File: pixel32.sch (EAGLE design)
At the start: 63 parts, among them CON1 DS1066-07M-SIDE, CON2 DS1066-07M-SIDE, CON3 PINHEAD_1X02-2.54, IC1 STM32F030K6TX-LQFP32(7X7), IC2 TPS54260, IC3 ST3485SOIC8, IC4 ESDA6V1L, IC5 3.3, IC6 MC74VHC1GT125, IC7 MC74VHC1GT125

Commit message: BLAH
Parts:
- removed C22: 1nF 1000V, rc:C-1206
- removed C25: 10uF 6.3V, rc:C-1206
- removed D4: SMF05C, pixel_masterlib:SMF05C
- removed D5: SMAJ12A, masterlib:SMAJ12A
- removed IC4: ESDA6V1L, pixel_masterlib:ESDA6V1L
- removed NRF24L01: NRF24L01, ali_modules:NRF24L01
- removed SJ1: (no value), eth_conv_master_lib:SOLDER_JOINT
- added C18: 100 nF, rc:C-0603
- added C27: 4.7u, rc:C-0805
- added C28: 0.1u, rc:C-0805
- added D1: SMF05C, pixel_masterlib:SMF05C
- added IC8: LM317, masterlib:LM317
- added R10, R13: (no value), rc:R-0805
- added R14, R15: 10K, rc:R-0603
- added SJ3, SJ4: (no value), eth_conv_master_lib:SOLDER_JOINT
- added U$6: CONNECTION, usb2can_master_lib:CONNECTION
- R11, R12: value 22R -> 100R
- R5: value 60R -> 120R
- R6: value 560R -> 1K; device rc:R-0603 -> rc:R-0805
- R7: value 560R -> 5K6; device rc:R-0603 -> rc:R-0805
- R9: value 60R -> 10K
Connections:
- removed net N$16: R5.1, R9.2, SJ1.1
- removed net N$17: C22.1, SJ1.2
- removed net N$18: R9.1, SJ2.2
- removed net NRF_CE: NRF24L01.CE
- removed net NRF_CSN: NRF24L01.CSN
- removed net NRF_IRQ: NRF24L01.IRQ
- new net GNDD: CON1.7, CON2.7, U$6.P$1
- new net LED_ANODE: C1.2, D1.C
- new net N$1: R5.1, SJ2.2
- new net N$20: IC8.ADJ, R6.1, R7.2
- new net VIN_SENSE: C18.2, R10.2, R13.2
- net A: now also D1.D2; no longer D5.P$1, IC4.C1, R6.2
- net B: now also D1.D1; no longer D5.P$2, IC4.C2, R7.1
- net CLOCK: now also D1.D4; no longer D4.D4, NRF24L01.SCK
- net CS: now also D1.D5; no longer D4.D5
- net CURRENT_SENS: no longer C1.1
- net DATA: now also D1.D3; no longer D4.D3
- net GND: now also C18.1, C27.1, C28.1, D1.G, R13.1, R14.1, R15.1, R7.1, R9.1, U$6.P$2; no longer C22.2, C25.2, CON1.7, CON2.7, D4.G, IC4.A, NRF24L01.GND, R6.1
- net LED1_PWM: now also R9.2
- net LED2_PWM: now also R14.2
- net LED3_PWM: now also R15.2
- net LED_CATHODE: now also C1.1; no longer C1.2
- net MISO: no longer NRF24L01.MISO
- net MOSI/DATA: no longer NRF24L01.MOSI
- net N$2: now also D1.A
- net N$3: now also LED_ANODE.P, R10.1, SJ3.1, SJ4.2
- net RS485_A: now also R12.2; no longer R11.2
- net RS485_B: now also R11.2; no longer R12.2
- net VDD_12V: now also C27.2, IC8.OUT, R6.2, SJ3.2; no longer LED_ANODE.P
- net VDD_24V: now also C28.2, IC8.IN, SJ4.1
- net VDD_3V3: no longer C25.1, NRF24L01.VCC, R7.2
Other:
- note added: "8.25V output"
- note removed: "OPTIONAL NRF24L01"
- moved on the sheet: C26, C5, C6, CON3, D3, LED_ANODE, LED_CATHODE1, LED_CATHODE2, LED_CATHODE3, R11, R12, R8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

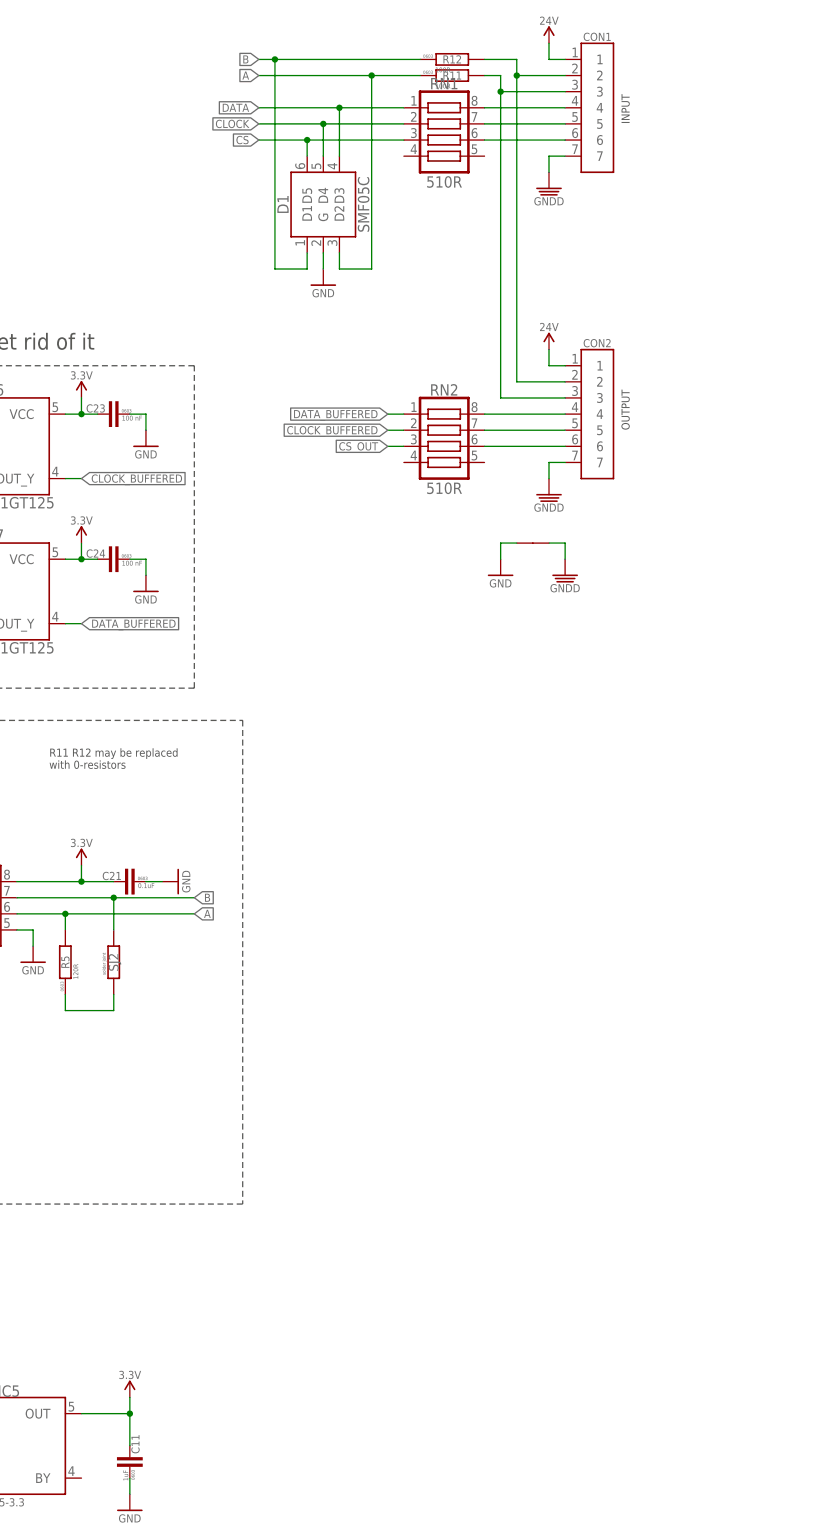
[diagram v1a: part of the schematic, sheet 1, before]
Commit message: First attempts in routing
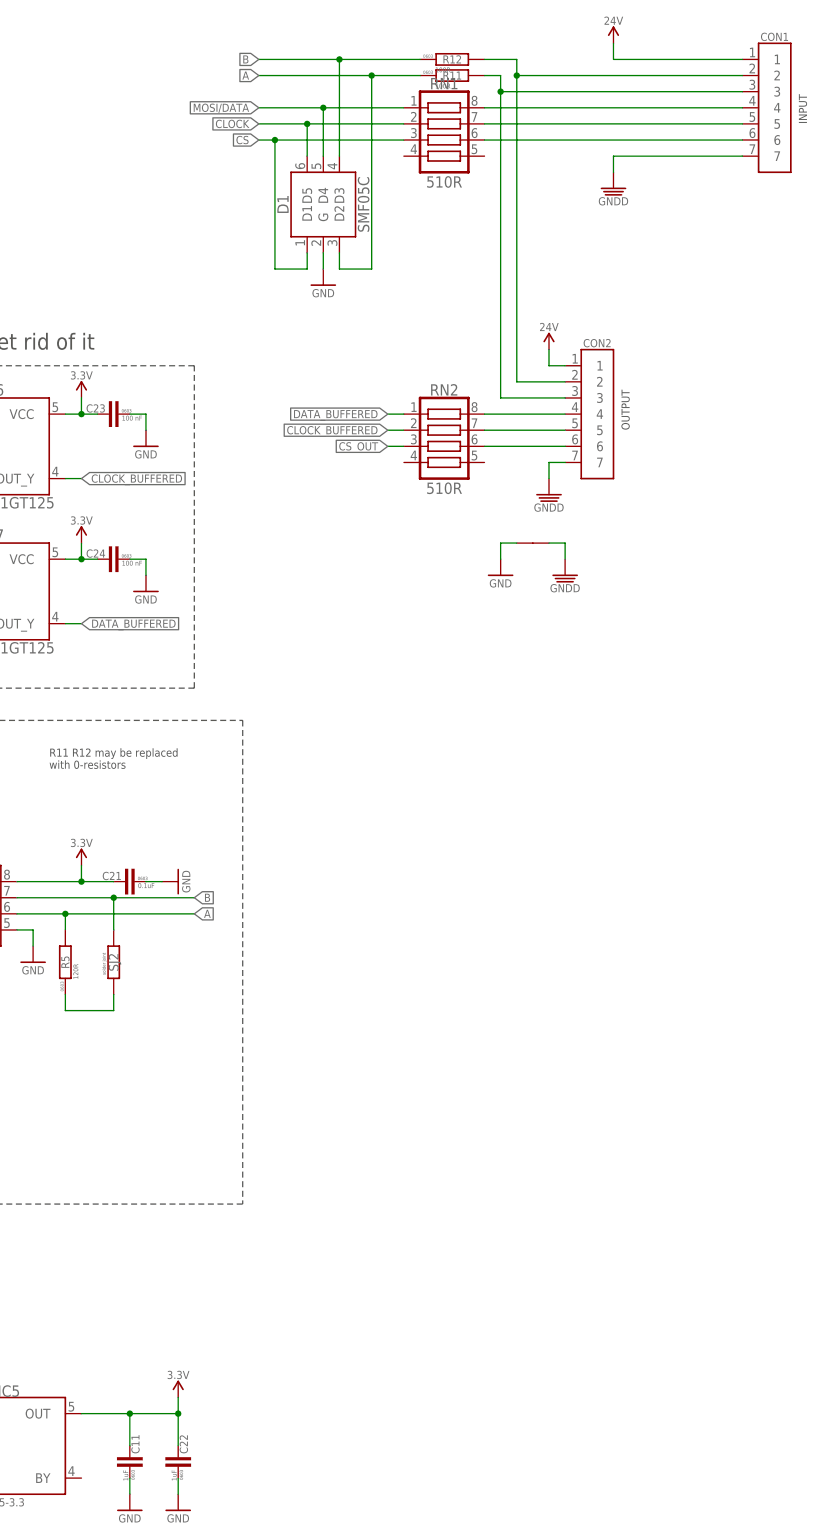
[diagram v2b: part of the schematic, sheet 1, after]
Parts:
- added C22: 1uF, rc:C-0603
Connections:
- removed net DATA: D1.D3, RN1.1
- net B: now also D1.D3; no longer D1.D1
- net CLOCK: now also D1.D5; no longer D1.D4
- net CS: now also D1.D1; no longer D1.D5
- net GND: now also C22.1
- net MOSI/DATA: now also D1.D4, RN1.1
- net VDD_3V3: now also C22.2
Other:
- moved on the sheet: CON1

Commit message: blah
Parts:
- removed C1: 0.1uF, rc:C-0603
- removed C10, C11, C22: 1uF, rc:C-0603
- removed C2, C3: 4.7u, rc:C-1210
- removed C4: 10n, rc:C-0603
- removed C5, C6: 47u 16V, rc:C-1210
- removed C7, C8: 18pF, rc:C-0603
- removed C9: 4700p, rc:C-0603
- removed D3: B360B-SMB, eth_conv_master_lib:B360B-SMB
- removed IC2: TPS54260, eth_conv_master_lib:TPS54260
- removed IC5: 3.3, gradus_mater_lib:LP2985-3.3V
- removed L1: 3R3, eth_conv_master_lib:L
- removed R1: 100K, rc:R-0603
- removed R2, R3: XXX, rc:R-0603
- removed R4: 18K 1%, rc:R-0603
- removed SJ4: (no value), eth_conv_master_lib:SOLDER_JOINT
- added SJ1: (no value), eth_conv_master_lib:SOLDER_JOINT
- C27, C28: device rc:C-0805 -> rc:C-1206
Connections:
- removed net AA: C1.2, D3.C, IC2.PH, L1.P$1
- removed net CURRENT_SENS: C3.2, R2.2
- removed net FB: IC2.VSENSE, R2.2, R3.1
- removed net LED_CATHODE: C1.1
- removed net N$6: C4.2, IC2.SS/TR
- removed net N$7: IC2.RT/CLK, R1.2
- removed net N$8: C9.2, R4.1
- net CLOCK: now also RN1.3; no longer RN1.2
- net CS: now also RN1.4; no longer RN1.3
- net CS_OUT: now also IC1.PA11, RN2.4; no longer IC1.PB6, RN2.3
- net GND: no longer C10.1, C11.1, C2.1, C22.1, C3.1, C4.1, C5.1, C6.1, C7.2, C8.2, C9.1, D3.A, IC2.GND, IC5.GND, R1.1, R2.1
- net LED_ANODE: no longer C1.2
- net MOSI/DATA: now also RN1.2; no longer RN1.1
- net N$11: now also RN1.7; no longer RN1.8
- net N$12: now also RN1.6; no longer RN1.7
- net N$13: now also RN1.5; no longer RN1.6
- net N$19: now also RN2.5; no longer RN2.6
- net N$2: no longer C1.1, IC2.BOOT
- net N$3: no longer LED_ANODE.P, R1.1, R10.1, R3.2, SJ3.1, SJ4.2
- net N$5: now also C28.2, IC8.IN, SJ1.2, SJ3.2; no longer C7.1, C8.1, IC2.COMP, R4.2
- net PWM: no longer R3.1
- net VDD_12V: now also SJ1.1; no longer C10.2, C2.2, C27.2, C5.2, C6.2, IC5.EN, IC5.IN, IC8.OUT, L1.P$2, R3.2, R6.2, SJ3.2
- net VDD_24V: now also LED_ANODE.P, R10.1, SJ3.1; no longer C2.2, C28.2, C3.2, IC2.VIN, IC8.IN, SJ4.1
- net VDD_3V3: now also C27.2, IC8.OUT, R6.2; no longer C11.2, C22.2, IC5.OUT
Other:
- note removed: "8.25V output"
- note removed: "C7 and C12 are here to reduce BOM"
- note removed: "Only option1 OR option2 should be placed"
- note removed: "Option 2"
- note removed: "Option1 will have max input V 60V"
- note removed: "Option2 will have max input V 25V. But its cheaper and easier"
- note removed: "Pull EN below 1.2V to disable Float to enable"
- note removed: "R11 R12 may be replaced with 0-resistors"
- moved on the sheet: C18, C21, C27, C28, CON1, D1, IC8, MODULE1, R10, R13, R6, R7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

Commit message: blah
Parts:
- removed C12: 100 nF, rc:C-0603
- added CON4: PINHEAD_1X03-2.54, pinhead:PINHEAD_1X03-2.54
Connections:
- removed net SYS_SWCLK: IC1.PA14
- removed net SYS_SWDIO: IC1.PA13
- net CS_OUT: now also IC1.PA12; no longer IC1.PA11
- net GND: now also CON4.2; no longer C12.1
- net N$2: now also CON4.1, IC1.PA14
- net N$3: now also CON4.3, IC1.PA13
- net VDD_3V3: no longer C12.2
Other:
- moved on the sheet: C13
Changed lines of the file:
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@@
 <part name="Q1" library="pixel_masterlib" deviceset="N-FET" device=""/>
 <part name="FRAME1" library="frames" deviceset="A5L-LOC" device=""/>
-<part name="C1" library="rc" deviceset="C" device="-1206" value="100 nF"/>
+<part name="C1" library="rc" deviceset="C" device="-1812" value="100 nF"/>
 </parts>
 <sheets>
@@
 <attribute name="BOM" x="88.9" y="93.98" size="1.778" layer="96" rot="R180" display="off"/>
 </instance>
-<instance part="TP3" gate="G$1" x="88.9" y="73.66" rot="R180">
-<attribute name="PARTNO" x="88.9" y="73.66" size="1.778" layer="96" rot="R180" display="off"/>
-<attribute name="BOM" x="88.9" y="73.66" size="1.778" layer="96" rot="R180" display="off"/>
+<instance part="TP3" gate="G$1" x="86.36" y="73.66" rot="R180">
+<attribute name="PARTNO" x="86.36" y="73.66" size="1.778" layer="96" rot="R180" display="off"/>
+<attribute name="BOM" x="86.36" y="73.66" size="1.778" layer="96" rot="R180" display="off"/>
 </instance>
 <instance part="+P1" gate="G$1" x="30.48" y="99.06"/>
@@
 <junction x="106.68" y="73.66"/>
 <pinref part="TP3" gate="G$1" pin="P$1"/>
-<wire x1="101.6" y1="73.66" x2="96.52" y2="73.66" width="0.1524" layer="91"/>
+<wire x1="101.6" y1="73.66" x2="93.98" y2="73.66" width="0.1524" layer="91"/>
 <pinref part="Q1" gate="G$1" pin="S"/>
 <wire x1="101.6" y1="81.28" x2="101.6" y2="73.66" width="0.1524" layer="91"/>
@@
 <part name="IC1" library="pixel_masterlib" deviceset="STM32F030K6TX" device="-LQFP32(7X7)"/>
 <part name="GND2" library="supply_symbols" deviceset="GND" device="" value="GND"/>
-<part name="C12" library="rc" deviceset="C" device="-0603" value="100 nF"/>
 <part name="C13" library="rc" deviceset="C" device="-0603" value="100 nF"/>
 <part name="C14" library="rc" deviceset="C" device="-0603" value="1 uF"/>
@@
 <part name="+P4" library="supply_symbols" deviceset="12V" device=""/>
 <part name="+P14" library="supply_symbols" deviceset="24V" device=""/>
+<part name="CON4" library="pinhead" deviceset="PINHEAD_1X03" device="-2.54"/>
+<part name="GND1" library="supply_symbols" deviceset="GND" device="" value="GND"/>
 </parts>
 <sheets>
@@
 <instance part="IC1" gate="IC" x="66.04" y="187.96"/>
 <instance part="GND2" gate="1" x="43.18" y="193.04"/>
-<instance part="C12" gate="G$1" x="55.88" y="228.6"/>
-<instance part="C13" gate="G$1" x="55.88" y="223.52"/>
+<instance part="C13" gate="G$1" x="55.88" y="226.06"/>
 <instance part="C14" gate="G$1" x="43.18" y="200.66" rot="R90"/>
 <instance part="C15" gate="G$1" x="48.26" y="200.66" rot="R90"/>
-<instance part="GND5" gate="1" x="50.8" y="218.44"/>
+<instance part="GND5" gate="1" x="50.8" y="220.98"/>
 <instance part="+P5" gate="G$1" x="43.18" y="208.28"/>
 <instance part="GND6" gate="1" x="48.26" y="193.04"/>
@@
 <instance part="R12" gate="G$1" x="322.58" y="241.3"/>
 <instance part="GND26" gate="1" x="256.54" y="99.06"/>
-<instance part="+P9" gate="G$1" x="60.96" y="231.14" rot="MR0"/>
+<instance part="+P9" gate="G$1" x="60.96" y="228.6" rot="MR0"/>
 <instance part="GND29" gate="1" x="274.32" y="96.52"/>
 <instance part="+P10" gate="G$1" x="264.16" y="114.3" rot="MR0"/>
@@
 <instance part="GND22" gate="G$1" x="337.82" y="172.72" rot="MR0"/>
 <instance part="GND23" gate="G$1" x="347.98" y="218.44" rot="MR0"/>
+<instance part="CON4" gate="G$1" x="134.62" y="220.98" rot="R180"/>
+<instance part="GND1" gate="1" x="116.84" y="215.9" rot="MR90"/>
 </instances>
 <busses>
@@
 </segment>
 <segment>
-<pinref part="C12" gate="G$1" pin="2"/>
 <pinref part="C13" gate="G$1" pin="2"/>
 <pinref part="IC1" gate="IC" pin="VDD@1"/>
 <wire x1="63.5" y1="215.9" x2="60.96" y2="215.9" width="0.1524" layer="91"/>
-<wire x1="60.96" y1="215.9" x2="60.96" y2="223.52" width="0.1524" layer="91"/>
+<wire x1="60.96" y1="215.9" x2="60.96" y2="226.06" width="0.1524" layer="91"/>
 <pinref part="+P9" gate="G$1" pin="VDD_3V3"/>
-<wire x1="58.42" y1="228.6" x2="60.96" y2="228.6" width="0.1524" layer="91"/>
-<wire x1="60.96" y1="228.6" x2="60.96" y2="231.14" width="0.1524" layer="91"/>
-<junction x="60.96" y="228.6"/>
-<wire x1="60.96" y1="223.52" x2="60.96" y2="228.6" width="0.1524" layer="91"/>
-<wire x1="58.42" y1="223.52" x2="60.96" y2="223.52" width="0.1524" layer="91"/>
-<junction x="60.96" y="223.52"/>
+<wire x1="60.96" y1="226.06" x2="60.96" y2="228.6" width="0.1524" layer="91"/>
+<wire x1="58.42" y1="226.06" x2="60.96" y2="226.06" width="0.1524" layer="91"/>
+<junction x="60.96" y="226.06"/>
 </segment>
 <segment>
@@
 <pinref part="GND5" gate="1" pin="GND"/>
 <pinref part="C13" gate="G$1" pin="1"/>
-<wire x1="53.34" y1="223.52" x2="50.8" y2="223.52" width="0.1524" layer="91"/>
-<wire x1="50.8" y1="223.52" x2="50.8" y2="220.98" width="0.1524" layer="91"/>
-<pinref part="C12" gate="G$1" pin="1"/>
-<wire x1="53.34" y1="228.6" x2="50.8" y2="228.6" width="0.1524" layer="91"/>
-<wire x1="50.8" y1="228.6" x2="50.8" y2="223.52" width="0.1524" layer="91"/>
-<junction x="50.8" y="223.52"/>
+<wire x1="53.34" y1="226.06" x2="50.8" y2="226.06" width="0.1524" layer="91"/>
+<wire x1="50.8" y1="226.06" x2="50.8" y2="223.52" width="0.1524" layer="91"/>
 </segment>
 <segment>
@@
 <wire x1="330.2" y1="165.1" x2="330.2" y2="162.56" width="0.1524" layer="91"/>
 </segment>
+<segment>
+<pinref part="CON4" gate="G$1" pin="2"/>
+<pinref part="GND1" gate="1" pin="GND"/>
+<wire x1="119.38" y1="215.9" x2="127" y2="215.9" width="0.1524" layer="91"/>
+</segment>
 </net>
 <net name="N$4" class="0">
@@
 <pinref part="RN1" gate="G$1" pin="3"/>
 <wire x1="299.72" y1="228.6" x2="314.96" y2="228.6" width="0.1524" layer="91"/>
-</segment>
-</net>
-<net name="SYS_SWDIO" class="0">
-<segment>
-<pinref part="IC1" gate="IC" pin="PA13"/>
-<wire x1="106.68" y1="213.36" x2="109.22" y2="213.36" width="0.1524" layer="91"/>
-<label x="109.22" y="213.36" size="1.27" layer="95" rot="MR180" xref="yes"/>
-</segment>
-</net>
-<net name="SYS_SWCLK" class="0">
-<segment>
-<pinref part="IC1" gate="IC" pin="PA14"/>
-<wire x1="106.68" y1="215.9" x2="109.22" y2="215.9" width="0.1524" layer="91"/>
-<label x="109.22" y="215.9" size="1.27" layer="95" rot="MR180" xref="yes"/>
 </segment>
 </net>
@@
 </segment>
 <segment>
-<pinref part="IC1" gate="IC" pin="PA11"/>
-<wire x1="106.68" y1="208.28" x2="109.22" y2="208.28" width="0.1524" layer="91"/>
-<label x="109.22" y="208.28" size="1.27" layer="95" xref="yes"/>
+<pinref part="IC1" gate="IC" pin="PA12"/>
+<wire x1="106.68" y1="210.82" x2="109.22" y2="210.82" width="0.1524" layer="91"/>
+<label x="109.22" y="210.82" size="1.27" layer="95" xref="yes"/>
 </segment>
 </net>
@@
 </segment>
 </net>
+<net name="N$2" class="0">
+<segment>
+<pinref part="IC1" gate="IC" pin="PA14"/>
+<wire x1="106.68" y1="215.9" x2="111.76" y2="215.9" width="0.1524" layer="91"/>
+<wire x1="111.76" y1="215.9" x2="111.76" y2="218.44" width="0.1524" layer="91"/>
+<pinref part="CON4" gate="G$1" pin="1"/>
+<wire x1="111.76" y1="218.44" x2="127" y2="218.44" width="0.1524" layer="91"/>
+</segment>
+</net>
+<net name="N$3" class="0">
+<segment>
+<pinref part="IC1" gate="IC" pin="PA13"/>
+<pinref part="CON4" gate="G$1" pin="3"/>
+<wire x1="106.68" y1="213.36" x2="127" y2="213.36" width="0.1524" layer="91"/>
+</segment>
+</net>
